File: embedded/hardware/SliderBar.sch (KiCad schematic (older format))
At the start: 35 parts, among them J1 USB_B_Mini, J2 MOTOR_OUT, J3 POT_IN, J4 DEBUG, U1 MIC5205-3.3YM5, U2 TB6612FNG, U3 MT3608, U4 STM32F072C8Tx

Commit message: Fix footprints
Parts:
- J2: footprint Connector_JST:JST_SH_SM02B-SRSS-TB_1x02-1MP_P1.00mm_Horizontal -> Connector_JST:JST_GH_SM02B-GHS-TB_1x02-1MP_P1.25mm_Horizontal
- J3: footprint Connector_JST:JST_SH_SM03B-SRSS-TB_1x03-1MP_P1.00mm_Horizontal -> Connector_JST:JST_GH_SM03B-GHS-TB_1x03-1MP_P1.25mm_Horizontal
- J4: footprint Connector_JST:JST_SH_SM05B-SRSS-TB_1x05-1MP_P1.00mm_Horizontal -> Connector_JST:JST_GH_SM05B-GHS-TB_1x05-1MP_P1.25mm_Horizontal
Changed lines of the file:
@@
 F 0 "J4" H 4230 4292 50  0000 L CNN
 F 1 "DEBUG" H 4230 4201 50  0000 L CNN
-F 2 "Connector_JST:JST_SH_SM05B-SRSS-TB_1x05-1MP_P1.00mm_Horizontal" H 4150 4250 50  0001 C CNN
+F 2 "Connector_JST:JST_GH_SM05B-GHS-TB_1x05-1MP_P1.25mm_Horizontal" H 4150 4250 50  0001 C CNN
 F 3 "~" H 4150 4250 50  0001 C CNN
 	1    4150 4250
@@
 F 0 "J2" H 4230 3092 50  0000 L CNN
 F 1 "MOTOR_OUT" H 4230 3001 50  0000 L CNN
-F 2 "Connector_JST:JST_SH_SM02B-SRSS-TB_1x02-1MP_P1.00mm_Horizontal" H 4150 3100 50  0001 C CNN
+F 2 "Connector_JST:JST_GH_SM02B-GHS-TB_1x02-1MP_P1.25mm_Horizontal" H 4150 3100 50  0001 C CNN
 F 3 "~" H 4150 3100 50  0001 C CNN
 	1    4150 3100
@@
 F 0 "J3" H 4230 3667 50  0000 L CNN
 F 1 "POT_IN" H 4230 3576 50  0000 L CNN
-F 2 "Connector_JST:JST_SH_SM03B-SRSS-TB_1x03-1MP_P1.00mm_Horizontal" H 4150 3625 50  0001 C CNN
+F 2 "Connector_JST:JST_GH_SM03B-GHS-TB_1x03-1MP_P1.25mm_Horizontal" H 4150 3625 50  0001 C CNN
 F 3 "~" H 4150 3625 50  0001 C CNN
 	1    4150 3625

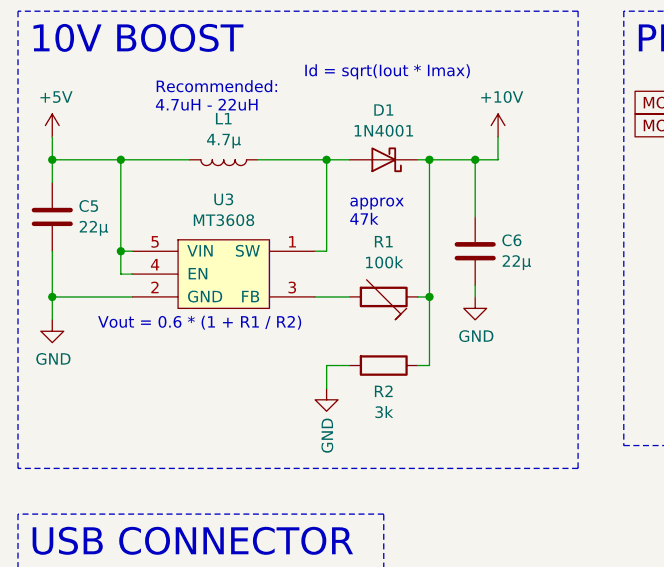
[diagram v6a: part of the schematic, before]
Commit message: Replace trimpot
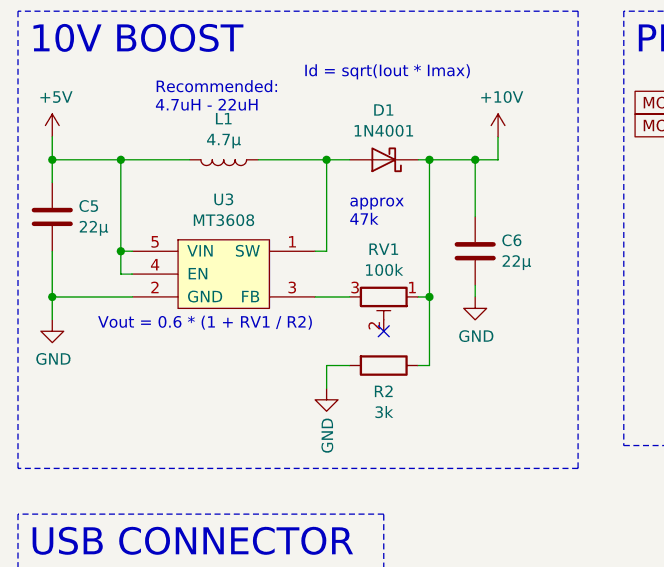
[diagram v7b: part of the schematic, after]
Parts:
- removed R1: 100k, ab2_passive:AB2_POT_TRIM, symbol Device:RTRIM
- added RV1: 100k, ab2_passive:AB2_POT_TRIM, symbol Device:R_POT_TRIM
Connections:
- net +10V: now also RV1.1
- net at U3.3 (FB): now also RV1.3
- no-connect marks 35 -> 36
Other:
- note added: "Vout = 0.6 * (1 + RV1 / R2)"
- note removed: "Vout = 0.6 * (1 + R1 / R2)"
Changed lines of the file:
@@
 Text Notes 2200 3650 0    50   ~ 0
 approx\n47k
-$Comp
-L Device:RTRIM R1
-U 1 1 5BCA1C5C
-P 2350 3950
-F 0 "R1" V 2110 3950 50  0000 C CNN
-F 1 "100k" V 2201 3950 50  0000 C CNN
-F 2 "ab2_passive:AB2_POT_TRIM" V 2280 3950 50  0001 C CNN
-F 3 "~" H 2350 3950 50  0001 C CNN
-	1    2350 3950
-	0    1    1    0
-$EndComp
 Wire Wire Line
 	2750 3900 2750 3950
@@
 $EndComp
 Text Notes 1100 4100 0    50   ~ 0
-Vout = 0.6 * (1 + R1 / R2)
+Vout = 0.6 * (1 + RV1 / R2)
 Text Notes 1350 3150 0    50   ~ 0
 Recommended:\n4.7uH - 22uH
@@
 Wire Wire Line
 	3000 1300 3150 1300
+$Comp
+L Device:R_POT_TRIM RV1
+U 1 1 5BDA4ED9
+P 2350 3950
+F 0 "RV1" V 2143 3950 50  0000 C CNN
+F 1 "100k" V 2234 3950 50  0000 C CNN
+F 2 "ab2_passive:AB2_POT_TRIM" H 2350 3950 50  0001 C CNN
+F 3 "~" H 2350 3950 50  0001 C CNN
+	1    2350 3950
+	0    1    1    0
+$EndComp
+NoConn ~ 2350 4100
 $EndSCHEMATC

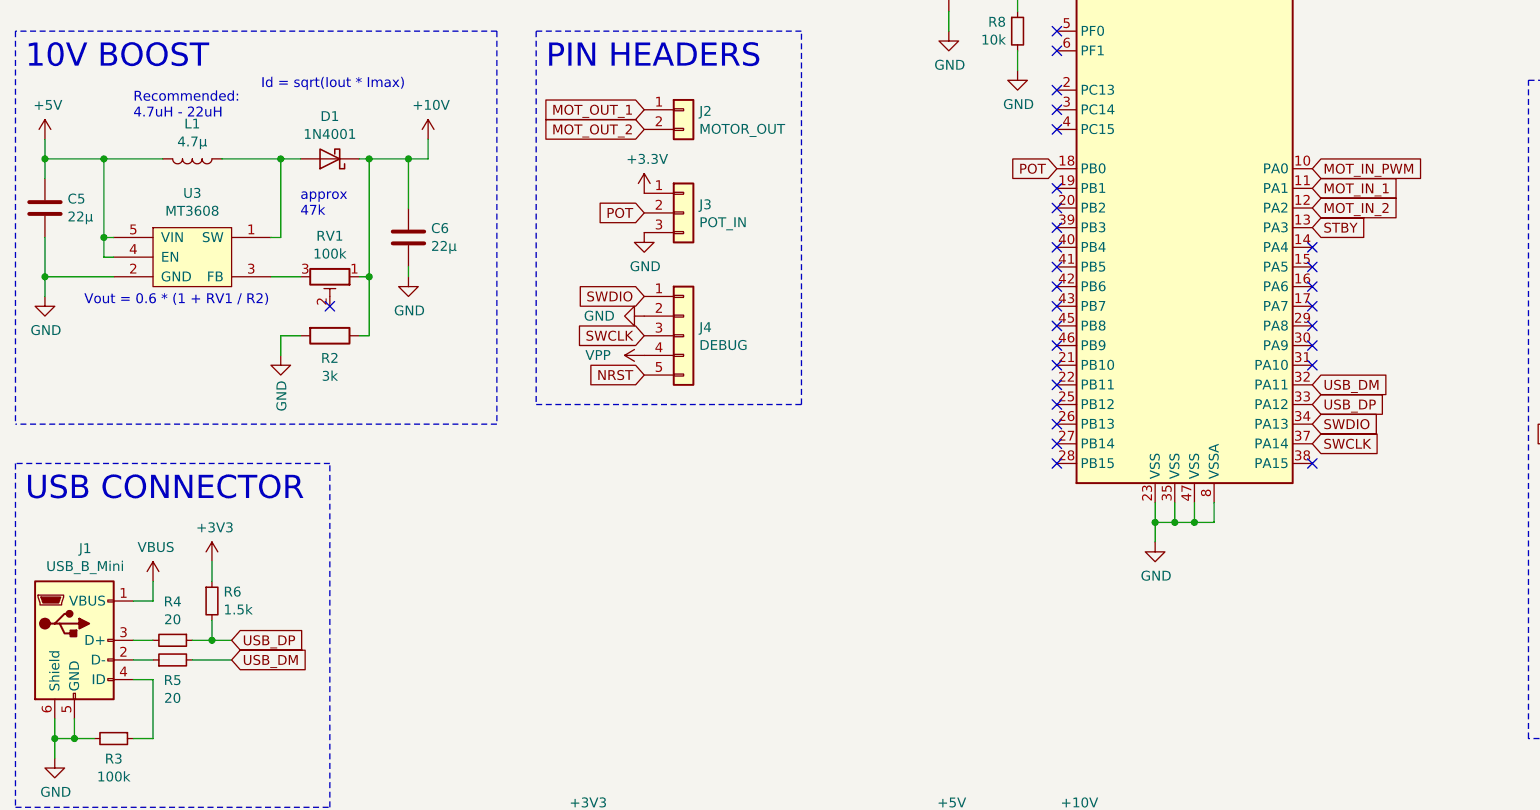
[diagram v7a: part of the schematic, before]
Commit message: Layout: motor driver, boost converter, 3.3v regulator, debug header, MCU, USB tracks
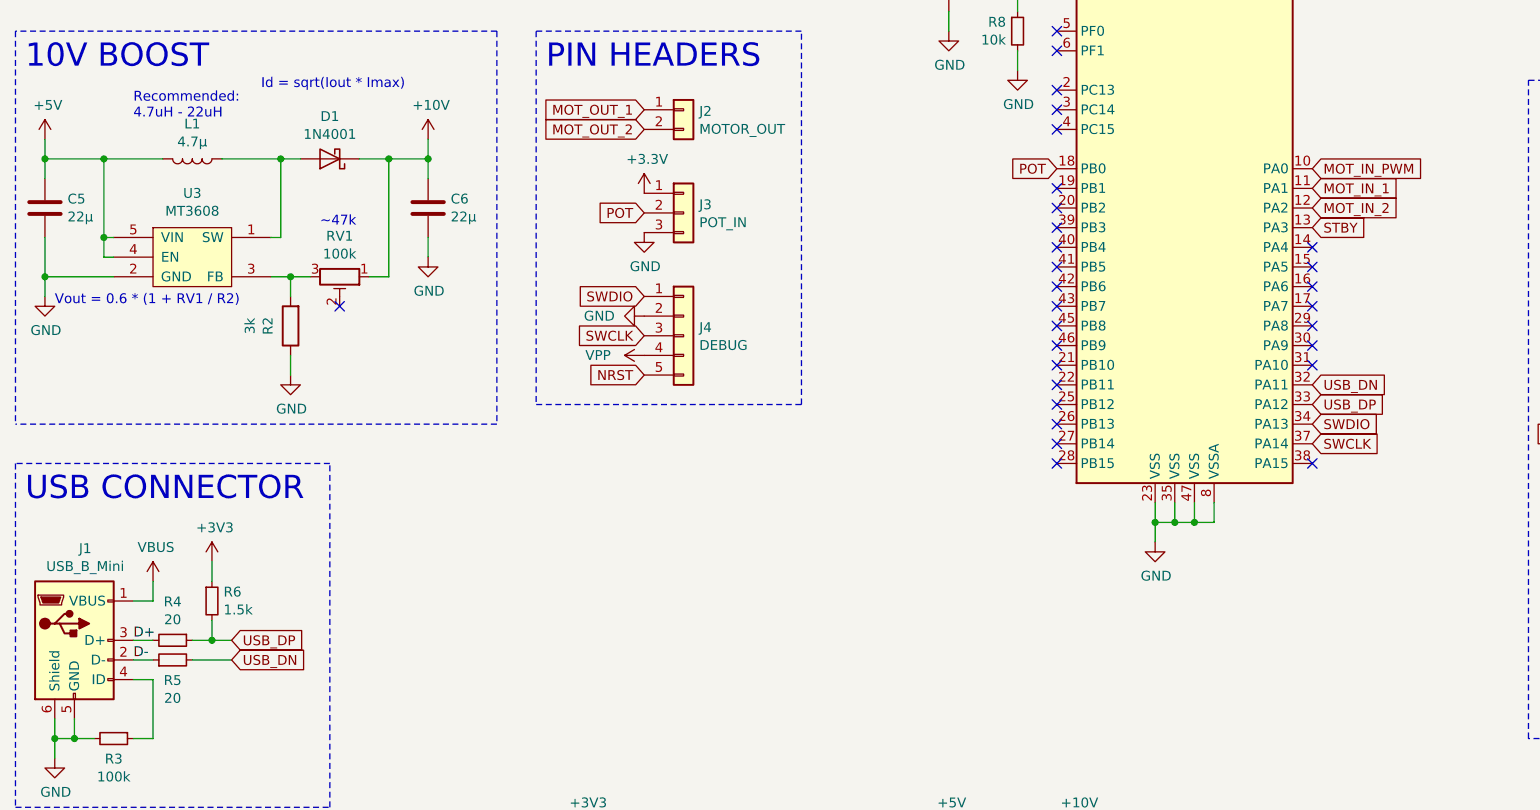
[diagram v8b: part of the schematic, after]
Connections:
- net +10V: no longer R2.1
- net GND: now also R2.1; no longer R2.2
- net at RV1.3, U3.3 (FB): now also R2.2
- net D+: now reaches J1.3 (D+), R4.2
- net D-: now reaches J1.2 (D-), R5.1
- net USB_DM renamed USB_DN
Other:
- note added: "~~47k"
- note removed: "approx\n47k"
- moved on the sheet: C6, R2, RV1
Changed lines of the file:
@@
 	1    0    0    -1
 $EndComp
-Text Notes 2200 3650 0    50   ~ 0
-approx\n47k
-Wire Wire Line
-	2750 3900 2750 3950
-Wire Wire Line
-	2750 3350 2550 3350
-Wire Wire Line
-	2750 3600 2750 3350
-Connection ~ 2750 3350
-Connection ~ 2550 3350
-Wire Wire Line
-	2550 3350 2500 3350
-Wire Wire Line
-	2500 4250 2550 4250
-Wire Wire Line
-	2550 4250 2550 3950
-Wire Wire Line
-	2550 3950 2550 3350
-Connection ~ 2550 3950
-Wire Wire Line
-	2500 3950 2550 3950
-Wire Wire Line
-	2200 3950 2050 3950
+Text Notes 2300 3700 0    50   ~ 0
+~~47k
 Wire Wire Line
 	2200 3350 2100 3350
@@
 L power:GND #PWR012
 U 1 1 5BC4D897
-P 2750 3950
-F 0 "#PWR012" H 2750 3700 50  0001 C CNN
-F 1 "GND" H 2755 3777 50  0000 C CNN
-F 2 "" H 2750 3950 50  0001 C CNN
-F 3 "" H 2750 3950 50  0001 C CNN
-	1    2750 3950
+P 2850 3850
+F 0 "#PWR012" H 2850 3600 50  0001 C CNN
+F 1 "GND" H 2855 3677 50  0000 C CNN
+F 2 "" H 2850 3850 50  0001 C CNN
+F 3 "" H 2850 3850 50  0001 C CNN
+	1    2850 3850
 	1    0    0    -1
 $EndComp
@@
 L Device:C C6
 U 1 1 5BC4B7C6
-P 2750 3750
-F 0 "C6" H 2635 3704 50  0000 R CNN
-F 1 "22µ" H 2635 3795 50  0000 R CNN
-F 2 "Capacitor_SMD:C_1206_3216Metric_Pad1.42x1.75mm_HandSolder" H 2788 3600 50  0001 C CNN
-F 3 "~" H 2750 3750 50  0001 C CNN
-	1    2750 3750
+P 2850 3600
+F 0 "C6" H 2735 3554 50  0000 R CNN
+F 1 "22µ" H 2735 3645 50  0000 R CNN
+F 2 "Capacitor_SMD:C_1206_3216Metric_Pad1.42x1.75mm_HandSolder" H 2888 3450 50  0001 C CNN
+F 3 "~" H 2850 3600 50  0001 C CNN
+	1    2850 3600
 	-1   0    0    1
 $EndComp
-Text Notes 1100 4100 0    50   ~ 0
+Text Notes 950  4100 0    50   ~ 0
 Vout = 0.6 * (1 + RV1 / R2)
 Text Notes 1350 3150 0    50   ~ 0
@@
 L power:GND #PWR011
 U 1 1 5BC48783
-P 2100 4350
-F 0 "#PWR011" H 2100 4100 50  0001 C CNN
-F 1 "GND" V 2105 4222 50  0000 R CNN
-F 2 "" H 2100 4350 50  0001 C CNN
-F 3 "" H 2100 4350 50  0001 C CNN
-	1    2100 4350
+P 2150 4450
+F 0 "#PWR011" H 2150 4200 50  0001 C CNN
+F 1 "GND" H 2155 4277 50  0000 C CNN
+F 2 "" H 2150 4450 50  0001 C CNN
+F 3 "" H 2150 4450 50  0001 C CNN
+	1    2150 4450
 	1    0    0    -1
 $EndComp
@@
 L Device:R R2
 U 1 1 5BC47906
-P 2350 4250
-F 0 "R2" V 2465 4250 50  0000 C CNN
-F 1 "3k" V 2556 4250 50  0000 C CNN
-F 2 "Resistor_SMD:R_1206_3216Metric_Pad1.42x1.75mm_HandSolder" V 2280 4250 50  0001 C CNN
-F 3 "~" H 2350 4250 50  0001 C CNN
-	1    2350 4250
-	0    1    1    0
+P 2150 4200
+F 0 "R2" V 2265 4200 50  0000 C CNN
+F 1 "3k" V 2356 4200 50  0000 C CNN
+F 2 "Resistor_SMD:R_1206_3216Metric_Pad1.42x1.75mm_HandSolder" V 2080 4200 50  0001 C CNN
+F 3 "~" H 2150 4200 50  0001 C CNN
+	1    2150 4200
+	-1   0    0    1
 $EndComp
 $Comp
@@
 	1    0    0    -1
 $EndComp
-Wire Wire Line
-	2850 3250 2850 3350
-Wire Wire Line
-	2750 3350 2850 3350
-Wire Wire Line
-	2100 4250 2100 4350
-Wire Wire Line
-	2100 4250 2200 4250
 Wire Notes Line width 12 style solid
 	3200 4700 750  4700
@@
 Connection ~ 3550 1300
 Text GLabel 7350 4500 2    50   Input ~ 0
-USB_DM
+USB_DN
 Text GLabel 7350 4600 2    50   Input ~ 0
 USB_DP
@@
 $EndComp
 Text GLabel 1850 5900 2    50   Input ~ 0
-USB_DM
+USB_DN
 Text GLabel 1850 5800 2    50   Input ~ 0
 USB_DP
@@
 L Device:R_POT_TRIM RV1
 U 1 1 5BDA4ED9
-P 2350 3950
-F 0 "RV1" V 2143 3950 50  0000 C CNN
-F 1 "100k" V 2234 3950 50  0000 C CNN
-F 2 "ab2_passive:AB2_POT_TRIM" H 2350 3950 50  0001 C CNN
-F 3 "~" H 2350 3950 50  0001 C CNN
-	1    2350 3950
+P 2400 3950
+F 0 "RV1" V 2193 3950 50  0000 C CNN
+F 1 "100k" V 2284 3950 50  0000 C CNN
+F 2 "ab2_passive:AB2_POT_TRIM" H 2400 3950 50  0001 C CNN
+F 3 "~" H 2400 3950 50  0001 C CNN
+	1    2400 3950
 	0    1    1    0
 $EndComp
-NoConn ~ 2350 4100
+NoConn ~ 2400 4100
+Wire Wire Line
+	2500 3350 2650 3350
+Wire Wire Line
+	2550 3950 2650 3950
+Wire Wire Line
+	2650 3950 2650 3350
+Wire Wire Line
+	2650 3350 2850 3350
+Wire Wire Line
+	2850 3350 2850 3250
+Connection ~ 2650 3350
+Wire Wire Line
+	2850 3350 2850 3450
+Connection ~ 2850 3350
+Wire Wire Line
+	2850 3750 2850 3850
+Wire Wire Line
+	2050 3950 2150 3950
+Wire Wire Line
+	2150 4350 2150 4450
+Wire Wire Line
+	2150 4050 2150 3950
+Connection ~ 2150 3950
+Wire Wire Line
+	2150 3950 2250 3950
+Text Label 1350 5800 0    50   ~ 0
+D+
+Text Label 1350 5900 0    50   ~ 0
+D-
 $EndSCHEMATC
